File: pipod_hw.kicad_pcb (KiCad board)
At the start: 4 copper layers, 55.5 x 96.8 mm, 141 parts, among them J3 Conn_01x03_Male, J7 USB_C_Receptacle_USB2.0, P1 FPC0.5MM14PPulltypeH2.0mmPick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, P2 FPC0.5MM8PPulltypeH2.0mmPickup, Q1 DMP1045U-7, Q2 UMW8205A, Q3 BSS138, Q4 TPNTK3139PT1G, U1 XC6210B332MR, U10 SY6283ADRC, U11 SY6283ADRC, U12 PCM5102, U13 PAM8908JER, U14 MCP23008-xML, U15 SY6283ADRC, U2 TP4056M, U3 DW01A-G, U4 MAX17048G+T10, U5 W25Q128JVS, U6 RP2040, U7 PI3USB102EZLEX, U8 TS3A5018RSVR, U9 SY6283ADRC, Y1 12MHz 20pF

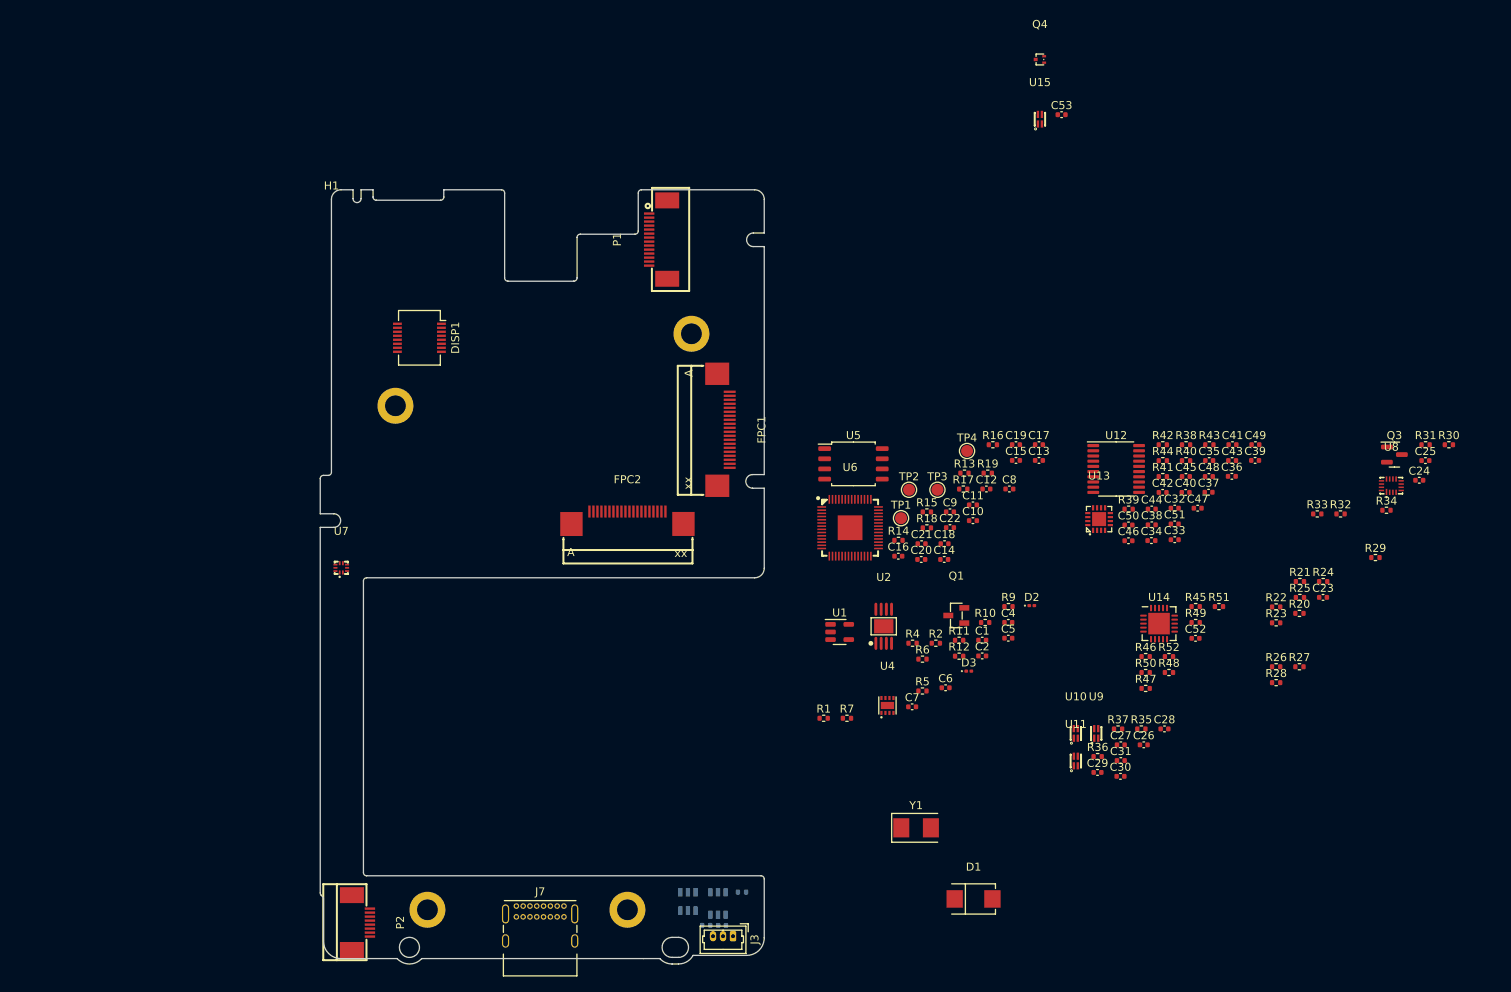
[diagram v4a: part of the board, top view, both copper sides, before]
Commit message: schem: migrate away from LCSC exclusive parts
- layout: migrate away from lcsc footprints
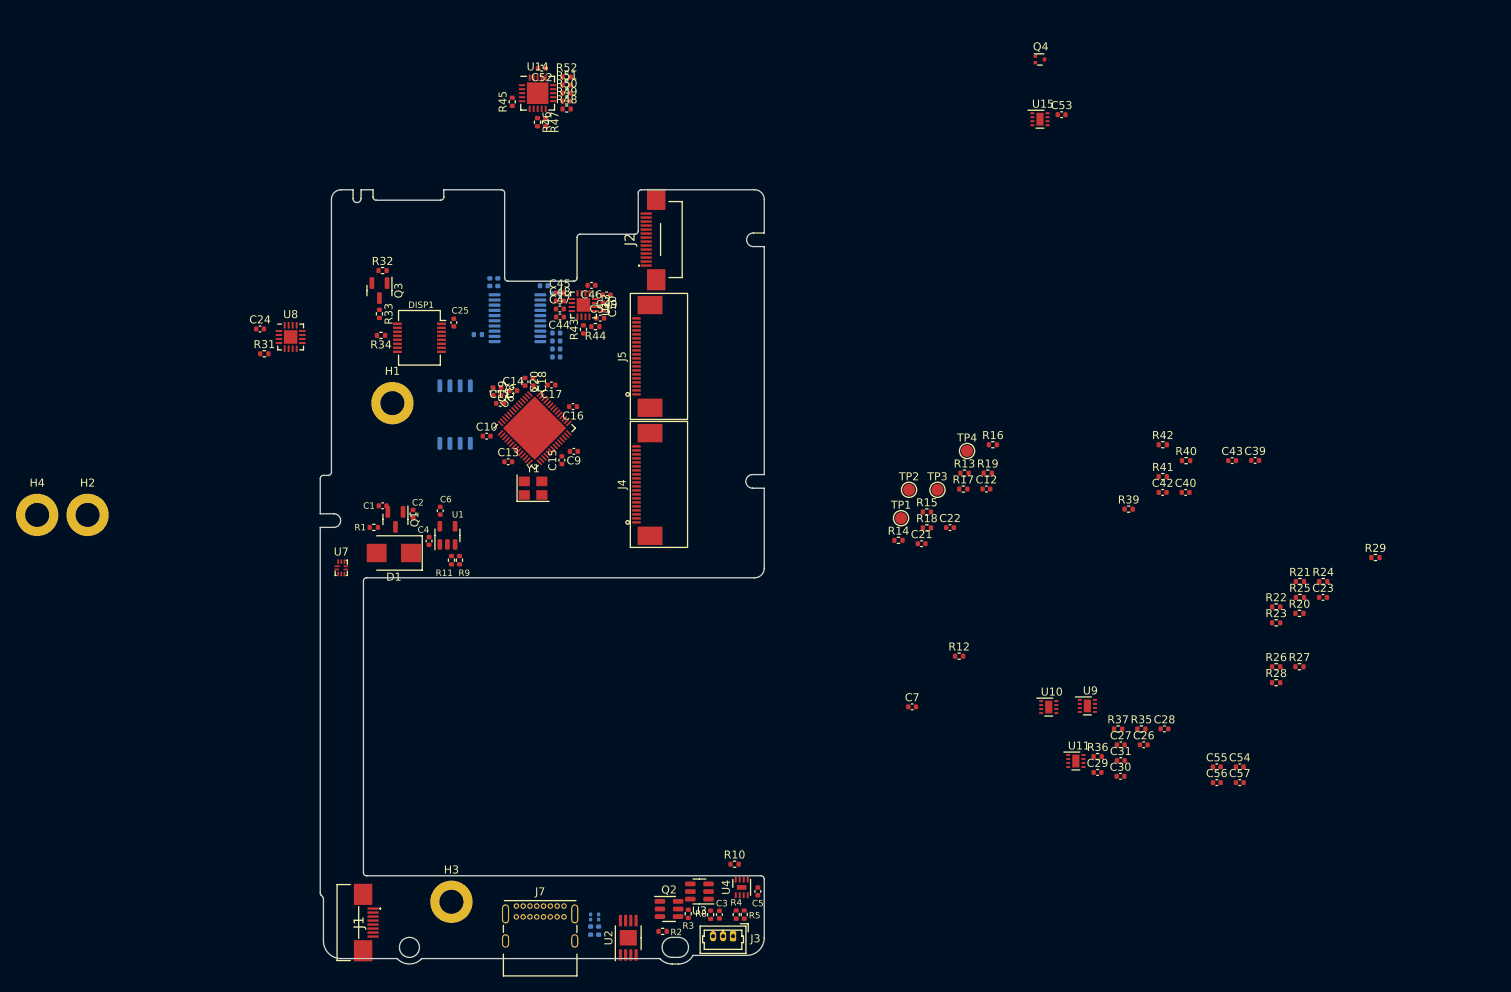
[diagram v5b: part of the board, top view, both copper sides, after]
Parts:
- removed FPC1, FPC2: 527462033, lcsc:FPC-SMD_527462033
- removed P1: FPC0.5MM14PPulltypeH2.0mmPickup, lcsc:FPC-SMD_14P-L12.5-W5.4-P0.50
- removed P2: FPC0.5MM8PPulltypeH2.0mmPickup, lcsc:FPC-SMD_AFC07-S08ECC-00
- removed R30: 0R, Resistor_SMD:R_0402_1005Metric
- added C54: DNI, Capacitor_SMD:C_0402_1005Metric, F.Cu at (113.5, 72.1)
- added C55: DNI, Capacitor_SMD:C_0402_1005Metric, F.Cu at (110.7, 72.1)
- added C56: DNI, Capacitor_SMD:C_0402_1005Metric, F.Cu at (110.7, 74.1)
- added C57: DNI, Capacitor_SMD:C_0402_1005Metric, F.Cu at (113.5, 74.1)
- added H2: 9774040243R, Gigahawk:9774040243R, F.Cu at (-30.5, 40.6)
- added H3: 9774040243R, Gigahawk:9774040243R, F.Cu at (15.0, 89.0)
- added H4: 9774040243R, Gigahawk:9774040243R, F.Cu at (-36.8, 40.6)
- added J1: SFV8R-2STE1HLF, Gigahawk:SFV8R2STE1HLF, F.Cu at (3.43, 91.6)
- added J2: SFV14R-2STE1HLF, Gigahawk:SFV14R2STE1HLF, F.Cu at (41.1, 6.22)
- added J4: 2-1734839-0, Gigahawk:2-1734839-0, F.Cu at (38.1, 36.8)
- added J5: 2-1734839-0, Gigahawk:2-1734839-0, F.Cu at (38.1, 20.8)
- C3, R3, R8: moved to F.Cu
- C32, C33, C34, C35, C36, C37, C38, C41, D2, D3, R38, R6, R7, U5: moved to B.Cu
- D1: footprint lcsc:SMB_L4.6-W3.6-LS5.3-RD -> Diode_SMD:D_SMB
- H1: value MountingHole_PiPod -> 9774040243R; footprint pipod_hw:MountingHole_PiPod -> Gigahawk:9774040243R
- Q1: footprint lcsc:SOT-23-3_L2.9-W1.3-P1.90-LS2.4-BR -> Package_TO_SOT_SMD:SOT-23
- Q2: footprint lcsc:SOT-23-6_L2.9-W1.6-P0.95-LS2.8-BL -> Package_TO_SOT_SMD:SOT-23-6; moved to F.Cu
- Q4: footprint lcsc:SOT-723_L1.2-W0.8-P0.40-LS1.2-BR -> Package_TO_SOT_SMD:SOT-723
- R34: value 0R -> 10k
- U10, U11, U15, U9: value SY6283ADRC -> TPS22965TDSGRQ1; footprint lcsc:DFN-4_L1.6-W1.2-P0.50-BL -> Package_SON:WSON-8-1EP_2x2mm_P0.5mm_EP0.9x1.6mm
- U12: value PCM5102 -> PCM5102APWR; moved to B.Cu
- U13: footprint lcsc:QFN-16_L3.0-W3.0-P0.50-BL-EP1.7 -> Package_DFN_QFN:QFN-16-1EP_3x3mm_P0.5mm_EP1.7x1.7mm
- U14: value MCP23008-xML -> MCP23008-E/ML
- U2: footprint lcsc:MSOP-8_L3.0-W3.0-P0.65-LS5.0-BL-EP -> Package_SO:MSOP-8-1EP_3x3mm_P0.65mm_EP1.95x2.15mm
- U3: footprint lcsc:SOT-23-6_L2.9-W1.6-P0.95-LS2.8-BR -> Package_TO_SOT_SMD:SOT-23-6; moved to F.Cu
- U4: footprint lcsc:DFN-8_L2.0-W2.0-P0.50-BL-EP -> Package_DFN_QFN:DFN-8-1EP_2x2mm_P0.5mm_EP0.6x1.2mm
- U6: footprint lcsc:LQFN-56_L7.0-W7.0-P0.4-EP -> Package_DFN_QFN:QFN-56-1EP_7x7mm_P0.4mm_EP5.6x5.6mm
- U7: value PI3USB102EZLEX -> NLAS7242MUTBG; footprint lcsc:TQFN-10_L1.6-W1.3-P0.50-BL -> Package_DFN_QFN:UQFN-10_1.4x1.8mm_P0.4mm
- U8: value TS3A5018RSVR -> RS2299XTQC16; footprint lcsc:UQFN-16_L2.6-W1.8-P0.40-BL -> Package_DFN_QFN:QFN-16-1EP_3x3mm_P0.5mm_EP1.7x1.7mm
- Y1: footprint Crystal:Crystal_SMD_5032-2Pin_5.0x3.2mm -> Crystal:Crystal_SMD_3225-4Pin_3.2x2.5mm
- moved C24 146.1 mm to (-8.92, 17.4)
- moved R31 145.6 mm to (-8.39, 20.5)
- moved U8 138.8 mm to (-5.10, 18.4)
- moved Q3 128.5 mm to (6.00, 12.6), turned to -90 degrees
- moved R34 127.6 mm to (6.20, 18.2), turned to 180 degrees
- moved R32 123.6 mm to (6.39, 10.1)
- moved C25 122.7 mm to (15.3, 16.6), turned to 90 degrees
- moved R33 119.9 mm to (6.00, 15.5), turned to -90 degrees
- moved C52 108.4 mm to (26.3, -15.2), turned to 180 degrees
- moved R45 106.2 mm to (22.6, -11.0), turned to 90 degrees
- moved R52 104.5 mm to (29.4, -14.1)
- moved R51 104.4 mm to (29.4, -13.1)
- moved R47 103.1 mm to (26.8, -8.45), turned to -90 degrees
- moved R48 103.1 mm to (29.4, -10.1)
- moved R50 102.4 mm to (29.4, -12.1)
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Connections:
- net Net-(R11-Pad2) renamed REG_CE
- net Net-(R2-Pad1) renamed /Power/CHRG_PROG
- C23 pad 1: VBUS -> +3V3
- U10 pad 1: GND -> VCC
- U10 pad 2: DISP_3V3_EN -> VCC
- U10 pad 3: +3V3 -> PI_VCC_EN
- U10 pad 4: DISP_3V3 -> VCC
- U11 pad 1: GND -> +3V3
- U11 pad 2: RMT_3V3_EN -> +3V3
- U11 pad 3: +3V3 -> DISP_3V3_EN
- U11 pad 4: HP_RMT4_3V3 -> +3V3
- U15 pad 1: GND -> +3V3
- U15 pad 2: PI_VCC_EN -> +3V3
- U15 pad 3: +3V3 -> RMT_3V3_EN
- U15 pad 4: AUDIO_3V3 -> +3V3
- U7 pad 9: VBUS -> +3V3
- U8 pad 1: PI_DISP_RST -> SMC_DISP_RST
- U8 pad 10: DISP_SCK -> DISP_INPUT_SEL
- U8 pad 12: SMC_DISP_SCK -> DISP_SCK
- U8 pad 13: Net-(R30-Pad2) -> SMC_DISP_SCK
- U8 pad 15: DISP_INPUT_SEL -> PI_DISP_RST
- U8 pad 16: SMC_DISP_RST -> DISP_RST
- U8 pad 2: DISP_RST -> DISP_INPUT_SEL
- U8 pad 3: SMC_DISP_DC -> PI_DISP_DC
- U8 pad 4: PI_DISP_DC -> DISP_DC
- U8 pad 5: DISP_DC -> SMC_DISP_DC
- U8 pad 7: DISP_MOSI -> PI_DISP_MOSI
- U8 pad 8: PI_DISP_MOSI -> DISP_MOSI
- U9 pad 1: GND -> +3V3
- U9 pad 2: PI_VCC_EN -> +3V3
- U9 pad 3: VCC -> PI_VCC_EN
- U9 pad 4: PI_VCC -> +3V3

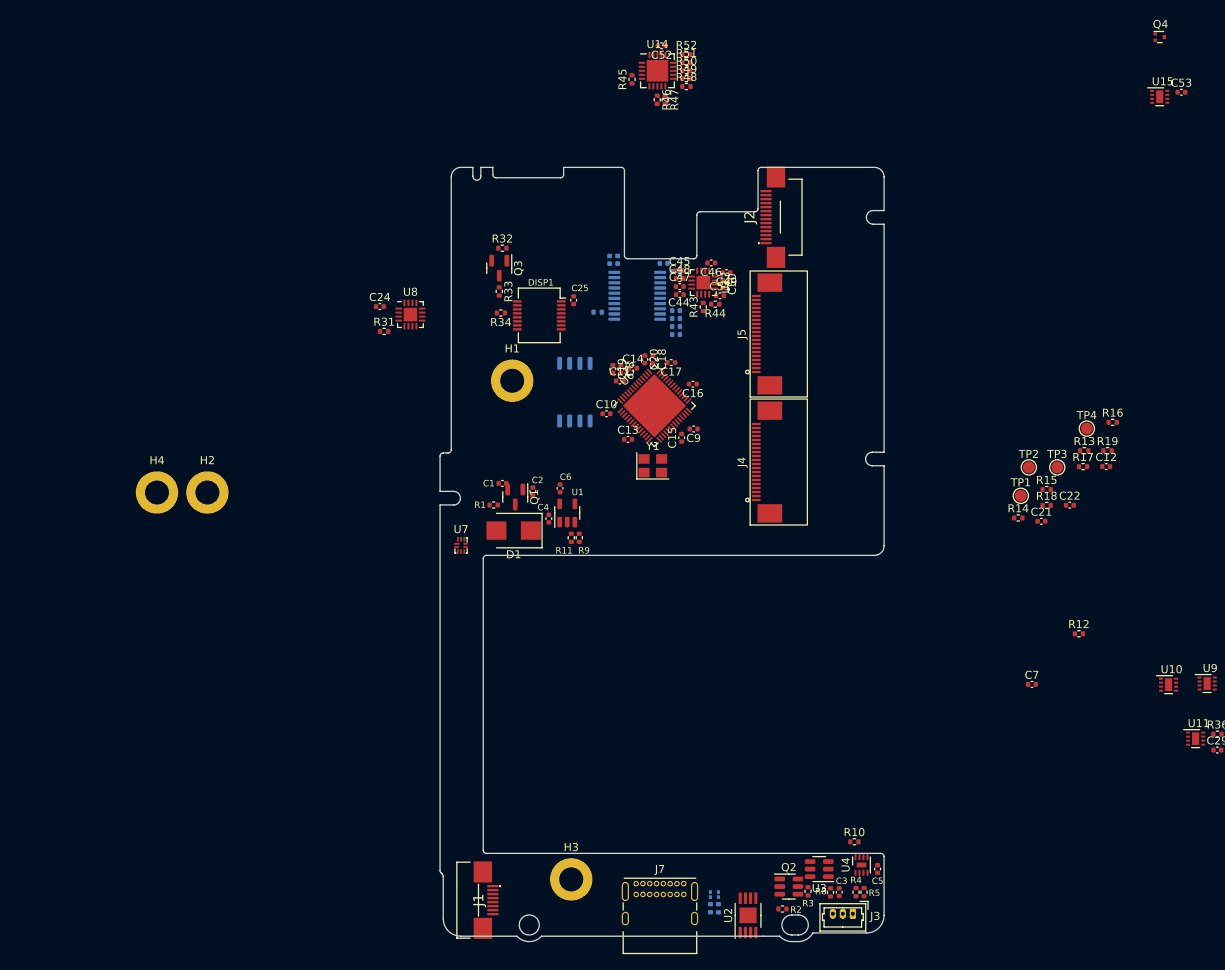
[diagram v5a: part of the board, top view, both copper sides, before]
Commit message: layout: update footprint for TP4056M
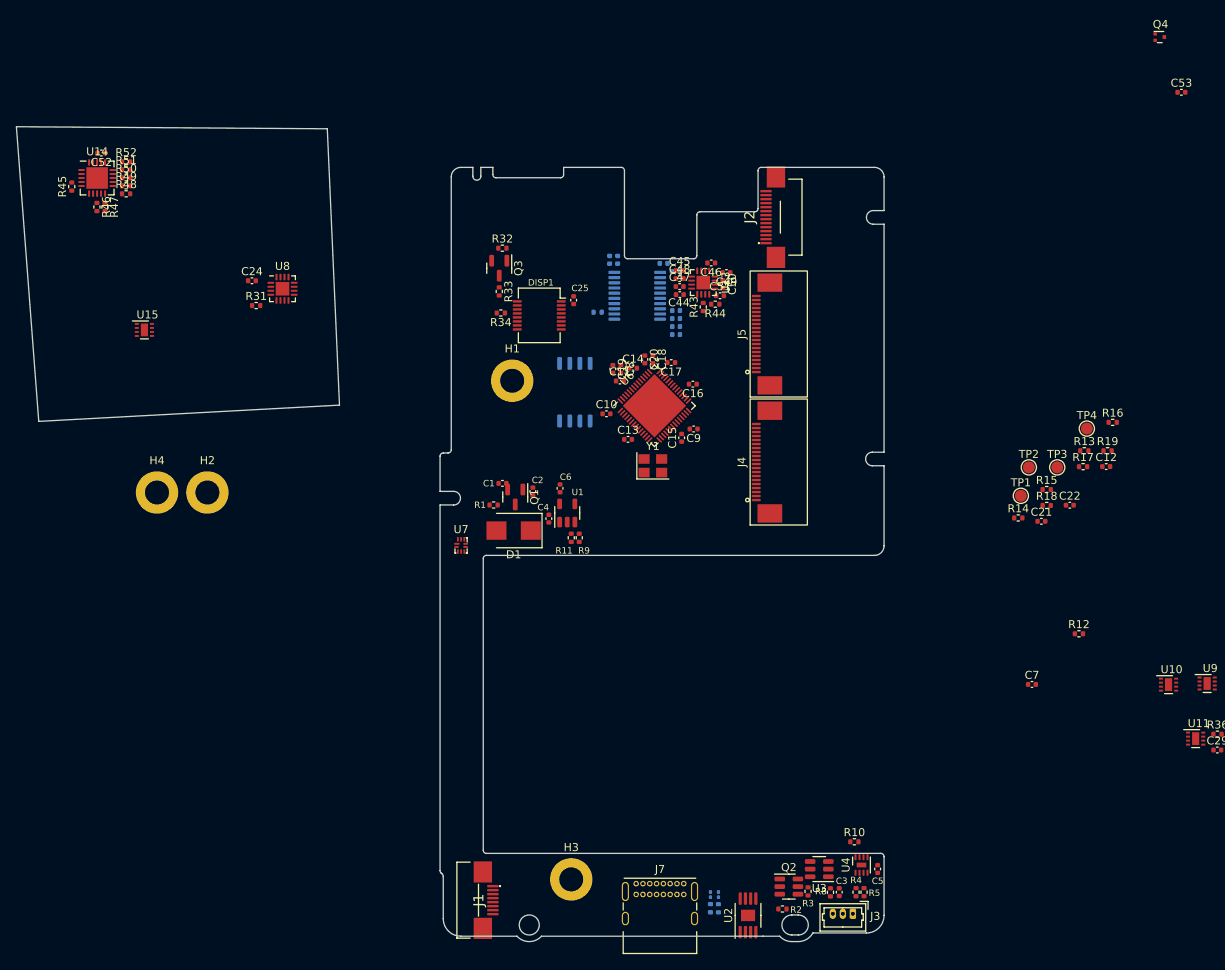
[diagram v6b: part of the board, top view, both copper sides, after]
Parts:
- U2: footprint Package_SO:MSOP-8-1EP_3x3mm_P0.65mm_EP1.95x2.15mm -> Gigahawk:MSOP-8-1EP_3x3mm_P0.65mm_EP1.425x1.76mm
- moved U15 130.2 mm to (-38.4, 20.3)
- moved C52 71.3 mm to (-43.7, -1.80)
- moved R45 71.3 mm to (-47.4, 2.40)
- moved R46 71.3 mm to (-44.3, 4.95)
- moved R47 71.3 mm to (-43.3, 4.95)
- moved R48 71.3 mm to (-40.6, 3.30)
- moved R49 71.3 mm to (-40.6, 2.30)
- moved R50 71.3 mm to (-40.6, 1.30)
- moved R51 71.3 mm to (-40.6, 0.30)
- moved R52 71.3 mm to (-40.6, -0.70)
- moved U14 71.3 mm to (-44.3, 1.33)
- moved R31 16.3 mm to (-24.4, 17.3)
- moved C24 16.3 mm to (-24.9, 14.2)
- moved U8 16.3 mm to (-21.1, 15.2)
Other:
- board size 55.5 x 96.8 mm -> 108.5 x 101.9 mm

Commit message: layout: preliminary layout of most of board
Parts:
- removed C44, C47: 1u, Capacitor_SMD:C_0402_1005Metric
- removed Q4: TPNTK3139PT1G, Package_TO_SOT_SMD:SOT-723
- removed R46, R47, R48, R49, R50, R51, R52: 0R, Resistor_SMD:R_0402_1005Metric
- removed R53: 10k, Resistor_SMD:R_0402_1005Metric
- added C58: 100n, Capacitor_SMD:C_0402_1005Metric, F.Cu at (16.0, 5.36)
- added L1: 1u, Inductor_SMD:L_Vishay_IFSC-1515AH_4x4x1.8mm, F.Cu at (31.1, 88.7)
- added R30: 10k, Resistor_SMD:R_0402_1005Metric, F.Cu at (24.7, 23.2)
- C12, C42, C43, C46, R39, R40, R41, R42, TP1, TP2, TP3, TP4: moved to B.Cu
- C2: value 100n -> 150n
- C29: value 10u -> DNI; moved to B.Cu
- C30, C31, C36: value 10u -> DNI
- C32, C34, R6: moved to F.Cu
- C33, C35, C37: value 100n -> 10u; moved to F.Cu
- C39: value 2.2u -> 100n; moved to B.Cu
- C4, C53: value 10u -> 1u
- C40: value 2.2u -> 10u; moved to B.Cu
- C45: value 1u -> 2.2u; moved to B.Cu
- C48: value 1u -> 10u; moved to B.Cu
- C49: value 1u -> 100n; moved to B.Cu
- C5: value 100n -> 10u
- C52: value 100n -> 2.2u
- C54, C55, C56, C57: value DNI -> 1u
- C6: value 10u -> 100n
- D1: value MBRS130LT3G -> RED; footprint Diode_SMD:D_SMB -> LED_SMD:LED_0402_1005Metric
- D2: value RED -> BLU; footprint LED_SMD:LED_0201_0603Metric -> LED_SMD:LED_0402_1005Metric; moved to F.Cu
- D3: footprint LED_SMD:LED_0201_0603Metric -> LED_SMD:LED_0402_1005Metric; moved to F.Cu
- Q1: value DMP1045U-7 -> DMG9926UDM; footprint Package_TO_SOT_SMD:SOT-23 -> Package_TO_SOT_SMD:SOT-23-6
- Q2: value UMW8205A -> NTK3139PT1G; footprint Package_TO_SOT_SMD:SOT-23-6 -> Package_TO_SOT_SMD:SOT-723
- R1: value 10k -> 5.9k 2%
- R10, R29: value 10k -> DNI
- R11: value DNI -> 2.2k
- R12: value DNI -> 10k; moved to B.Cu
- R13: value 10k -> DNP; moved to B.Cu
- R14: value DNP -> 1k
- R15, R3: value 1k -> 10k
- R16: value 10k -> 27R
- R18: value 27R -> 10k
- R19: value 10k -> DNP
- R2: value 1.62k 2% -> 1.6k
- R20: value DNP -> 10k
- R21: value 10k -> 15k
- R22: value 15k -> 5.1k
- R24: value 5.1k -> 10k
- R26: value 10k -> 100k
- R27: value 100k -> 10k
- R4: value 5.62k 2% -> 1k
- R5: value 1.27M 2% -> 1k
- R7: value 1k -> 10k; moved to F.Cu
- R8: value 470R -> 330R
- U1: value XC6210B332MR -> MAX17048G+T10; footprint Package_TO_SOT_SMD:SOT-23-5 -> Package_DFN_QFN:DFN-8-1EP_2x2mm_P0.5mm_EP0.6x1.2mm
- U12: value PCM5102APWR -> TPS22965TDSGRQ1; footprint Package_SO:TSSOP-20_4.4x6.5mm_P0.65mm -> Package_SON:WSON-8-1EP_2x2mm_P0.5mm_EP0.9x1.6mm; moved to F.Cu
- U13: value PAM8908JER -> PCM5102APWR; footprint Package_DFN_QFN:QFN-16-1EP_3x3mm_P0.5mm_EP1.7x1.7mm -> Package_SO:TSSOP-20_4.4x6.5mm_P0.65mm; moved to B.Cu
- U14: value MCP23008-E/ML -> PAM8908JER; footprint Package_DFN_QFN:QFN-20-1EP_4x4mm_P0.5mm_EP2.7x2.7mm -> Package_DFN_QFN:QFN-16-1EP_3x3mm_P0.5mm_EP1.7x1.7mm
- U15: value TPS22965TDSGRQ1 -> MCP23008-E/ML; footprint Package_SON:WSON-8-1EP_2x2mm_P0.5mm_EP0.9x1.6mm -> Package_DFN_QFN:QFN-20-1EP_4x4mm_P0.5mm_EP2.7x2.7mm
- U2: value TP4056M -> MAX8903AETI+T; footprint Gigahawk:MSOP-8-1EP_3x3mm_P0.65mm_EP1.425x1.76mm -> Package_DFN_QFN:QFN-28-1EP_4x4mm_P0.4mm_EP2.6x2.6mm
- U3: value DW01A-G -> BQ29728DSER; footprint Package_TO_SOT_SMD:SOT-23-6 -> Package_SON:WSON-6_1.5x1.5mm_P0.5mm
- U4: value MAX17048G+T10 -> XC6210B332MR; footprint Package_DFN_QFN:DFN-8-1EP_2x2mm_P0.5mm_EP0.6x1.2mm -> Package_TO_SOT_SMD:SOT-23-5
- moved C23 123.2 mm to (0.89, 46.2), turned to 90 degrees
- moved R24 122.6 mm to (1.38, 48.5), turned to 180 degrees
- moved R25 119.6 mm to (8.26, 90.8)
- moved R27 117.9 mm to (7.75, 92.3), turned to 90 degrees
- moved R21 111.2 mm to (17.5, 89.5), turned to 90 degrees
- moved R20 110.4 mm to (17.5, 91.5), turned to 90 degrees
- moved R28 104.9 mm to (19.7, 25.5), turned to 90 degrees
- moved C57 103.3 mm to (31.3, 11.5), turned to 90 degrees
- moved R22 102.9 mm to (21.6, 87.8), turned to 180 degrees
- moved C55 102.3 mm to (27.9, 12.0)
- moved C56 101.9 mm to (29.9, 12.0)
- moved R26 101.7 mm to (17.6, 43.9), turned to 180 degrees
- moved R29 100.8 mm to (36.4, 9.78)
- moved U11 100.7 mm to (4.23, 23.9)
- moved C54 100.4 mm to (29.1, 17.7), turned to 90 degrees
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- renumbered J3 to J1, J7 to J2, J1 to J3, J2 to J4, J4 to J6
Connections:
- C2 pad 1: VCC -> GND
- C2 pad 2: GND -> /Power/CHRG_TIMER_SET
- C26 pad 2: VCC -> +3V3
- C27 pad 2: PI_VCC -> VCC
- C29 pad 2: DISP_3V3 -> Net-(C29-Pad2)
- C3 pad 1: /Power/DW01A_VCC -> Net-(C3-Pad1)
- C3 pad 2: -BATT -> Net-(C3-Pad2)
- C30 pad 2: +3V3 -> Net-(C30-Pad2)
- C31 pad 2: HP_RMT4_3V3 -> Net-(C31-Pad2)
- C32 pad 1: AUDIO_3V3 -> GND
- C32 pad 2: GND -> PI_VCC
- C33 pad 1: AUDIO_3V3 -> GND
- C33 pad 2: GND -> DISP_3V3
- C34 pad 1: AUDIO_3V3 -> GND
- C34 pad 2: GND -> AUDIO_3V3
- C35 pad 1: AUDIO_3V3 -> GND
- C35 pad 2: GND -> +3V3
- C36 pad 1: AUDIO_3V3 -> GND
- C36 pad 2: GND -> Net-(C36-Pad2)
- C37 pad 1: AUDIO_3V3 -> GND
- C37 pad 2: GND -> HP_RMT4_3V3
- C39 pad 1: Net-(C39-Pad1) -> AUDIO_3V3
- C39 pad 2: Net-(C39-Pad2) -> GND
- C4 pad 2: VCC -> Net-(C4-Pad2)
- C40 pad 1: Net-(C40-Pad1) -> AUDIO_3V3
- C42 pad 1: Net-(C42-Pad1) -> AUDIO_3V3
- C43 pad 1: Net-(C42-Pad1) -> AUDIO_3V3
- C45 pad 1: DAC_OUTL -> Net-(C45-Pad1)
- C46 pad 1: GND -> Net-(C46-Pad1)
- C46 pad 2: AUDIO_3V3 -> GND
- C48 pad 1: GND -> Net-(C48-Pad1)
- C48 pad 2: Net-(C48-Pad2) -> GND
- C49 pad 1: GND -> Net-(C48-Pad1)
- C49 pad 2: Net-(C49-Pad2) -> GND
- C5 pad 2: +BATT -> VCC
- C50 pad 1: Net-(C50-Pad1) -> DAC_OUTR
- C51 pad 1: Net-(C51-Pad1) -> DAC_OUTL
- C51 pad 2: GND -> Net-(C51-Pad2)
- C53 pad 2: AUDIO_3V3 -> Net-(C53-Pad2)
- C56 pad 1: GND -> Net-(C56-Pad1)
- C57 pad 1: GND -> Net-(C57-Pad1)
- C57 pad 2: Net-(C57-Pad2) -> GND
- C6 pad 1: +3V3 -> /Power/PROT_BAT+
- C6 pad 2: GND -> -BATT
- C7 pad 1: GND -> +3V3
- C7 pad 2: +3V3 -> GND
- D1 pad 1: VCC -> Net-(D1-Pad1)
- J2 pad S1: Net-(J7-PadS1) -> Net-(J2-PadS1)
- J4 pad 2: Net-(J2-Pad2) -> /Headphone/HP_CLICKER_SPEAKER
- J5 pad 10: PI_VCC -> HP_SL_VIDEO
- J5 pad 11: PI_VCC -> SMC_PI_I2C_SDA
- J5 pad 12: PI_VCC -> SMC_PI_I2C_SCL
- J5 pad 13: PI_VCC -> SMC_TX_PI_RX
- J5 pad 14: PI_VCC -> SMC_RX_PI_TX
- J5 pad 15: PI_VCC -> SMC_INT
- J5 pad 16: GND -> PI_USB_MUXED_D+
- J5 pad 17: GND -> PI_USB_MUXED_D-
- J5 pad 3: GND -> PI_I2S_BCK
- J5 pad 4: GND -> PI_I2S_DIN
- J5 pad 5: GND -> PI_I2S_LRCK
- J5 pad 6: PI_VCC -> PI_DISP_RST
- J5 pad 7: PI_VCC -> PI_DISP_DC
- J5 pad 8: PI_VCC -> PI_DISP_MOSI
- J5 pad 9: PI_VCC -> PI_DISP_SCK
- J6 pad 10: HP_SL_VIDEO -> PI_VCC
- J6 pad 11: SMC_PI_I2C_SDA -> PI_VCC
- J6 pad 12: SMC_PI_I2C_SCL -> PI_VCC
- J6 pad 13: SMC_TX_PI_RX -> PI_VCC
- J6 pad 14: SMC_RX_PI_TX -> PI_VCC
- J6 pad 15: SMC_INT -> PI_VCC
- J6 pad 16: PI_USB_MUXED_D+ -> GND
- J6 pad 17: PI_USB_MUXED_D- -> GND
- J6 pad 3: PI_I2S_BCK -> GND
- J6 pad 4: PI_I2S_DIN -> GND
- J6 pad 5: PI_I2S_LRCK -> GND
- J6 pad 6: PI_DISP_RST -> PI_VCC
- J6 pad 7: PI_DISP_DC -> PI_VCC
- J6 pad 8: PI_DISP_MOSI -> PI_VCC
- J6 pad 9: PI_DISP_SCK -> PI_VCC
- Q1 pad 1: VBUS -> GND
- Q1 pad 2: VCC -> Net-(Q1-Pad2)
- Q1 pad 3: +BATT -> -BATT
- Q2 pad 1: GND -> HP_CLICKER
- Q2 pad 2: unconnected-(Q2-Pad2) -> +3V3
- Q2 pad 3: -BATT -> /Headphone/HP_CLICKER_SPEAKER
- R1 pad 2: VBUS -> /Power/CHRG_IN_CURR_SET
- R10 pad 1: +3V3 -> GND
- R10 pad 2: ~{FG_ALRT} -> REG_CE
- R11 pad 2: REG_CE -> Net-(R11-Pad2)
- R12 pad 1: HP_CLICKER -> /SMC/~{SMC_USB_BOOT}
- R12 pad 2: Net-(J2-Pad2) -> ~{SMC_QSPI_SS}
- R13 pad 1: /SMC/~{SMC_USB_BOOT} -> ~{SMC_QSPI_SS}
- R13 pad 2: ~{SMC_QSPI_SS} -> +3V3
- R14 pad 1: ~{SMC_QSPI_SS} -> Net-(R14-Pad1)
- R14 pad 2: +3V3 -> Net-(C22-Pad1)
- R15 pad 1: Net-(R15-Pad1) -> +3V3
- R15 pad 2: Net-(C22-Pad1) -> MCU_RUN
- R16 pad 1: +3V3 -> SMC_USB_MUXED_D+
- R16 pad 2: MCU_RUN -> /SMC/SMC_USB_D+
- R17 pad 1: SMC_USB_MUXED_D+ -> SMC_USB_MUXED_D-
- R17 pad 2: /SMC/SMC_USB_D+ -> /SMC/SMC_USB_D-
- R18 pad 1: SMC_USB_MUXED_D- -> /SMC/~{SMC_CW_CS}
- R18 pad 2: /SMC/SMC_USB_D- -> GND
- R19 pad 1: /SMC/~{SMC_CW_CS} -> GND
- R19 pad 2: GND -> Net-(J2-PadS1)
- R2 pad 1: /Power/CHRG_PROG -> GND
- R2 pad 2: GND -> /Power/CHRG_CURR_SET
- R20 pad 1: GND -> VBUS
- R20 pad 2: Net-(J7-PadS1) -> USB_DET
- R21 pad 1: VBUS -> USB_DET
- R21 pad 2: USB_DET -> GND
- R22 pad 1: USB_DET -> USB_CC1
- R23 pad 1: USB_CC1 -> USB_CC2
- R24 pad 1: USB_CC2 -> USB_MUX_SEL
- R24 pad 2: GND -> +3V3
- R25 pad 1: USB_MUX_SEL -> CW_EN1
- R25 pad 2: GND -> +3V3
- R26 pad 1: CW_EN1 -> SMC_CW_MOSI
- R27 pad 1: SMC_CW_MOSI -> CW_EN2
- R28 pad 1: CW_EN2 -> HP_LCK
- R29 pad 1: HP_LCK -> HP_CLICKER
- R29 pad 2: +3V3 -> /Headphone/HP_CLICKER_SPEAKER
- R3 pad 1: GND -> +3V3
- R3 pad 2: /Power/CS -> ~{FG_ALRT}
- R4 pad 1: NTC -> Net-(D1-Pad1)
- R4 pad 2: VBUS -> ~{CHRG_FLT}
- R5 pad 1: GND -> Net-(D2-Pad1)
- R5 pad 2: NTC -> ~{CHRG}
- R6 pad 1: ~{CHRG} -> Net-(D3-Pad1)
- R6 pad 2: Net-(D2-Pad1) -> ~{CHRG_DOK}
- R7 pad 1: ~{CHRG_SB} -> Net-(C4-Pad2)
- R7 pad 2: Net-(D3-Pad1) -> NTC
- R8 pad 1: /Power/DW01A_VCC -> +BATT
- R8 pad 2: +BATT -> /Power/PROT_BAT+
- U1 pad 1: VCC -> GND
- U1 pad 2: GND -> +BATT
- U1 pad 3: REG_CE -> +BATT
- U1 pad 4: unconnected-(U1-Pad4) -> GND
- U1 pad 5: +3V3 -> ~{FG_ALRT}
- U10 pad 6: Net-(C55-Pad2) -> Net-(C30-Pad2)
- U11 pad 6: Net-(C56-Pad2) -> Net-(C31-Pad2)
- U12 pad 1: AUDIO_3V3 -> +3V3
- U12 pad 2: Net-(C39-Pad1) -> +3V3
- U12 pad 3: GND -> RMT_3V3_EN
- U12 pad 4: Net-(C39-Pad2) -> +3V3
- U12 pad 5: Net-(C40-Pad1) -> GND
- U12 pad 6: DAC_OUTL -> Net-(C36-Pad2)
- U12 pad 7: DAC_OUTR -> HP_RMT4_3V3
- U12 pad 8: AUDIO_3V3 -> HP_RMT4_3V3
- U13 pad 1: Net-(C45-Pad2) -> AUDIO_3V3
- U13 pad 10: GND -> PI_DAC_DEMP
- U13 pad 11: Net-(C50-Pad1) -> PI_DAC_FLT
- U13 pad 12: Net-(C49-Pad2) -> Net-(R38-Pad2)
- U13 pad 13: PI_AMP_EN -> PI_I2S_BCK
- U13 pad 14: AUDIO_3V3 -> PI_I2S_DIN
- U13 pad 15: GNDA -> PI_I2S_LRCK
- U13 pad 16: HP_T_L -> PI_DAC_FMT
- U13 pad 17: GND -> PI_DAC_XSMT
- U13 pad 2: Net-(C48-Pad2) -> Net-(C45-Pad1)
- U13 pad 3: Net-(C47-Pad2) -> GND
- U13 pad 4: Net-(C44-Pad2) -> Net-(C45-Pad2)
- U13 pad 5: HP_R1_R -> Net-(C46-Pad1)
- U13 pad 6: PI_AMP_G0 -> DAC_OUTL
- U13 pad 7: PI_AMP_G1 -> DAC_OUTR
- U13 pad 8: Net-(C51-Pad1) -> AUDIO_3V3
- U13 pad 9: Net-(C50-Pad2) -> GND
- U14 pad 1: GND -> Net-(C51-Pad2)
- U14 pad 10: Net-(R47-Pad1) -> GND
- U14 pad 11: Net-(R48-Pad1) -> Net-(C56-Pad1)
- U14 pad 12: Net-(R49-Pad1) -> Net-(C55-Pad2)
- U14 pad 13: Net-(R50-Pad1) -> PI_AMP_EN
- U14 pad 14: Net-(R51-Pad1) -> AUDIO_3V3
- U14 pad 15: Net-(R52-Pad1) -> GNDA
- U14 pad 16: unconnected-(U14-Pad16) -> HP_T_L
- U14 pad 2: GND -> Net-(C54-Pad2)
- U14 pad 3: GND -> Net-(C53-Pad2)
- U14 pad 4: Net-(R45-Pad2) -> Net-(C50-Pad2)
- U14 pad 5: unconnected-(U14-Pad5) -> HP_R1_R
- U14 pad 6: unconnected-(U14-Pad6) -> PI_AMP_G0
- U14 pad 7: unconnected-(U14-Pad7) -> PI_AMP_G1
- U14 pad 8: unconnected-(U14-Pad8) -> Net-(C57-Pad1)
- U14 pad 9: Net-(R46-Pad1) -> Net-(C56-Pad2)
- U15 pad 1: +3V3 -> GND
- U15 pad 2: +3V3 -> GND
- U15 pad 3: RMT_3V3_EN -> GND
- U15 pad 4: +3V3 -> Net-(R45-Pad2)
- U15 pad 5: GND -> unconnected-(U15-Pad5)
- U15 pad 6: Net-(C57-Pad2) -> unconnected-(U15-Pad6)
- U15 pad 7: HP_RMT4_3V3 -> unconnected-(U15-Pad7)
- U15 pad 8: HP_RMT4_3V3 -> unconnected-(U15-Pad8)
- U15 pad 9: GND -> PI_AMP_EN
- U2 pad 1: NTC -> GND
- U2 pad 2: /Power/CHRG_PROG -> GND
- U2 pad 3: GND -> VBUS
- U2 pad 5: +BATT -> VBUS
- U2 pad 6: ~{CHRG_SB} -> Net-(C3-Pad2)
- U2 pad 7: ~{CHRG} -> VBUS
- U2 pad 8: VBUS -> ~{CHRG_DOK}
- U2 pad 9: GND -> Net-(C4-Pad2)
- U3 pad 1: /Power/OD -> unconnected-(U3-Pad1)
- U3 pad 2: /Power/CS -> /Power/PROT_C
- U3 pad 3: /Power/OC -> /Power/PROT_D
- U3 pad 4: unconnected-(U3-Pad4) -> -BATT
- U3 pad 5: /Power/DW01A_VCC -> /Power/PROT_BAT+
- U3 pad 6: -BATT -> Net-(R11-Pad2)
- U4 pad 1: GND -> VCC
- U4 pad 2: +BATT -> GND
- U4 pad 3: +BATT -> REG_CE
- U4 pad 4: GND -> unconnected-(U4-Pad4)
- U4 pad 5: ~{FG_ALRT} -> +3V3
- U6 pad 21: Net-(R15-Pad1) -> Net-(R14-Pad1)
- U6 pad 27: SMC_I2C_SDA -> SMC_INT
- U6 pad 28: SMC_I2C_SCL -> HP_CLICKER
- U6 pad 32: SMC_INT -> SMC_RMT_TX
- U6 pad 34: HP_CLICKER -> SMC_RMT_RX
- U6 pad 35: HP_LCK -> unconnected-(U6-Pad35)
- U6 pad 36: ~{FG_ALRT} -> HP_LCK
- U6 pad 5: unconnected-(U6-Pad5) -> ~{FG_ALRT}
- U6 pad 6: SMC_RMT_TX -> SMC_I2C_SDA
- U6 pad 7: SMC_RMT_RX -> SMC_I2C_SCL
- U7 pad 4: SMC_USB_MUXED_D- -> PI_USB_MUXED_D-
- U7 pad 5: SMC_USB_MUXED_D+ -> PI_USB_MUXED_D+
- U7 pad 6: PI_USB_MUXED_D- -> SMC_USB_MUXED_D-
- U7 pad 7: PI_USB_MUXED_D+ -> SMC_USB_MUXED_D+
- U9 pad 6: Net-(C54-Pad2) -> Net-(C29-Pad2)
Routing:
- net ~{FG_ALRT}: track 0.00 -> 140.7 mm, vias 0 -> 6
- net SMC_I2C_SDA: track 0.00 -> 121.4 mm, vias 0 -> 3
- net SMC_I2C_SCL: track 0.00 -> 120.3 mm, vias 0 -> 3
- net USB_DET: track 0.00 -> 100.3 mm, vias 0 -> 6
- net VCC: track 0.00 -> 96.3 mm, vias 0 -> 5
- net GND: track 0.00 -> 83.4 mm, vias 0 -> 39
- net SMC_CW_MOSI: track 0.00 -> 80.6 mm, vias 0 -> 2
- net SMC_CW_SCK: track 0.00 -> 80.1 mm, vias 0 -> 2
- net USB_D+: track 0.00 -> 63.3 mm, vias 0 -> 1
- net USB_D-: track 0.00 -> 63.3 mm, vias 0 -> 1
- net +3V3: track 0.00 -> 62.9 mm, vias 0 -> 11
- net AUDIO_3V3: track 0.00 -> 38.7 mm, vias 0 -> 4
- net VBUS: track 0.00 -> 31.4 mm, vias 0 -> 4
- net +BATT: track 0.00 -> 25.4 mm, vias 0 -> 1
- net SMC_USB_MUXED_D-: track 0.00 -> 22.7 mm, vias 0 -> 2
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- added copper zone on In2.Cu, net GND
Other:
- board size 108.5 x 101.9 mm -> 55.5 x 96.8 mm
